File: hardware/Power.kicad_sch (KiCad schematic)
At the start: 36 parts, among them J200 Conn_Receptacle_2P, J201 Solder pad, J202 Solder pad, J203 Solder pad, J204 Solder pad, Q200 AO3401A, SW200 SW_Push_Dual, SW201 SW_Push_Dual, SW202 MU-AS90R, U200 RT9080-33GJ5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

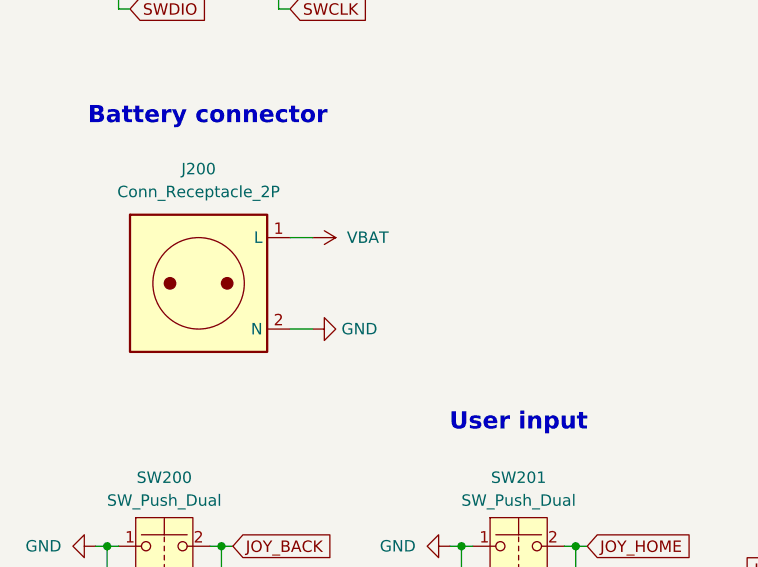
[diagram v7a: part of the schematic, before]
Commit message: Replace JST connector with PicoBlade 1.25 one
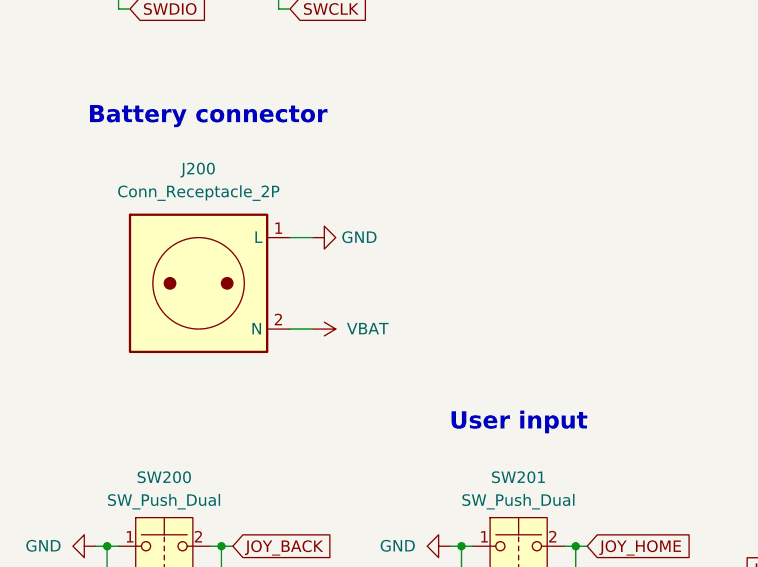
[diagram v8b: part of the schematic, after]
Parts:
- J200: footprint Connector_JST:JST_PH_S2B-PH-SM4-TB_1x02-1MP_P2.00mm_Horizontal -> Connector_Molex:Molex_PicoBlade_53261-0271_1x02-1MP_P1.25mm_Horizontal
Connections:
- net GND: now also J200.1 (L); no longer J200.2 (N)
- net VBAT: now also J200.2 (N); no longer J200.1 (L)
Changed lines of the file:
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@@
 	(symbol
 		(lib_id "power:GND")
-		(at 49.53 158.75 90)
+		(at 49.53 148.59 90)
 		(unit 1)
 		(exclude_from_sim no)
@@
 		(fields_autoplaced yes)
 		(property "Reference" "#PWR032"
-			(at 55.88 158.75 0)
+			(at 55.88 148.59 0)
 			(effects
 				(font
@@
 		)
 		(property "Value" "GND"
-			(at 52.705 158.7499 90)
+			(at 52.705 148.5899 90)
 			(effects
 				(font
@@
 		)
 		(property "Footprint" ""
-			(at 49.53 158.75 0)
+			(at 49.53 148.59 0)
 			(effects
 				(font
@@
 		)
 		(property "Datasheet" ""
-			(at 49.53 158.75 0)
+			(at 49.53 148.59 0)
 			(effects
 				(font
@@
 		)
 		(property "Description" ""
-			(at 49.53 158.75 0)
+			(at 49.53 148.59 0)
 			(effects
 				(font
@@
 			)
 		)
-		(property "Footprint" "Connector_JST:JST_PH_S2B-PH-SM4-TB_1x02-1MP_P2.00mm_Horizontal"
+		(property "Footprint" "Connector_Molex:Molex_PicoBlade_53261-0271_1x02-1MP_P1.25mm_Horizontal"
 			(at 32.258 153.924 0)
 			(effects
@@
 	(symbol
 		(lib_id "power:+3V3")
-		(at 49.53 148.59 270)
+		(at 49.53 158.75 270)
 		(unit 1)
 		(exclude_from_sim no)
@@
 		(dnp no)
 		(property "Reference" "#PWR031"
-			(at 45.72 148.59 0)
+			(at 45.72 158.75 0)
 			(effects
 				(font
@@
 		)
 		(property "Value" "VBAT"
-			(at 55.626 148.59 90)
+			(at 55.626 158.75 90)
 			(effects
 				(font
@@
 		)
 		(property "Footprint" ""
-			(at 49.53 148.59 0)
+			(at 49.53 158.75 0)
 			(effects
 				(font
@@
 		)
 		(property "Datasheet" ""
-			(at 49.53 148.59 0)
+			(at 49.53 158.75 0)
 			(effects
 				(font
@@
 		)
 		(property "Description" "Power symbol creates a global label with name \"+3V3\""
-			(at 49.53 148.59 0)
-			(effects
-				(font
+			(at 49.53 158.75 0)
+			(effects
+				(font
